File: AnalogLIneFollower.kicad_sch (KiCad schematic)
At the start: 28 parts, among them M1 Left Motor, M2 Right Motor, Q1 SS8050, Q2 SS8050, U1 LM358

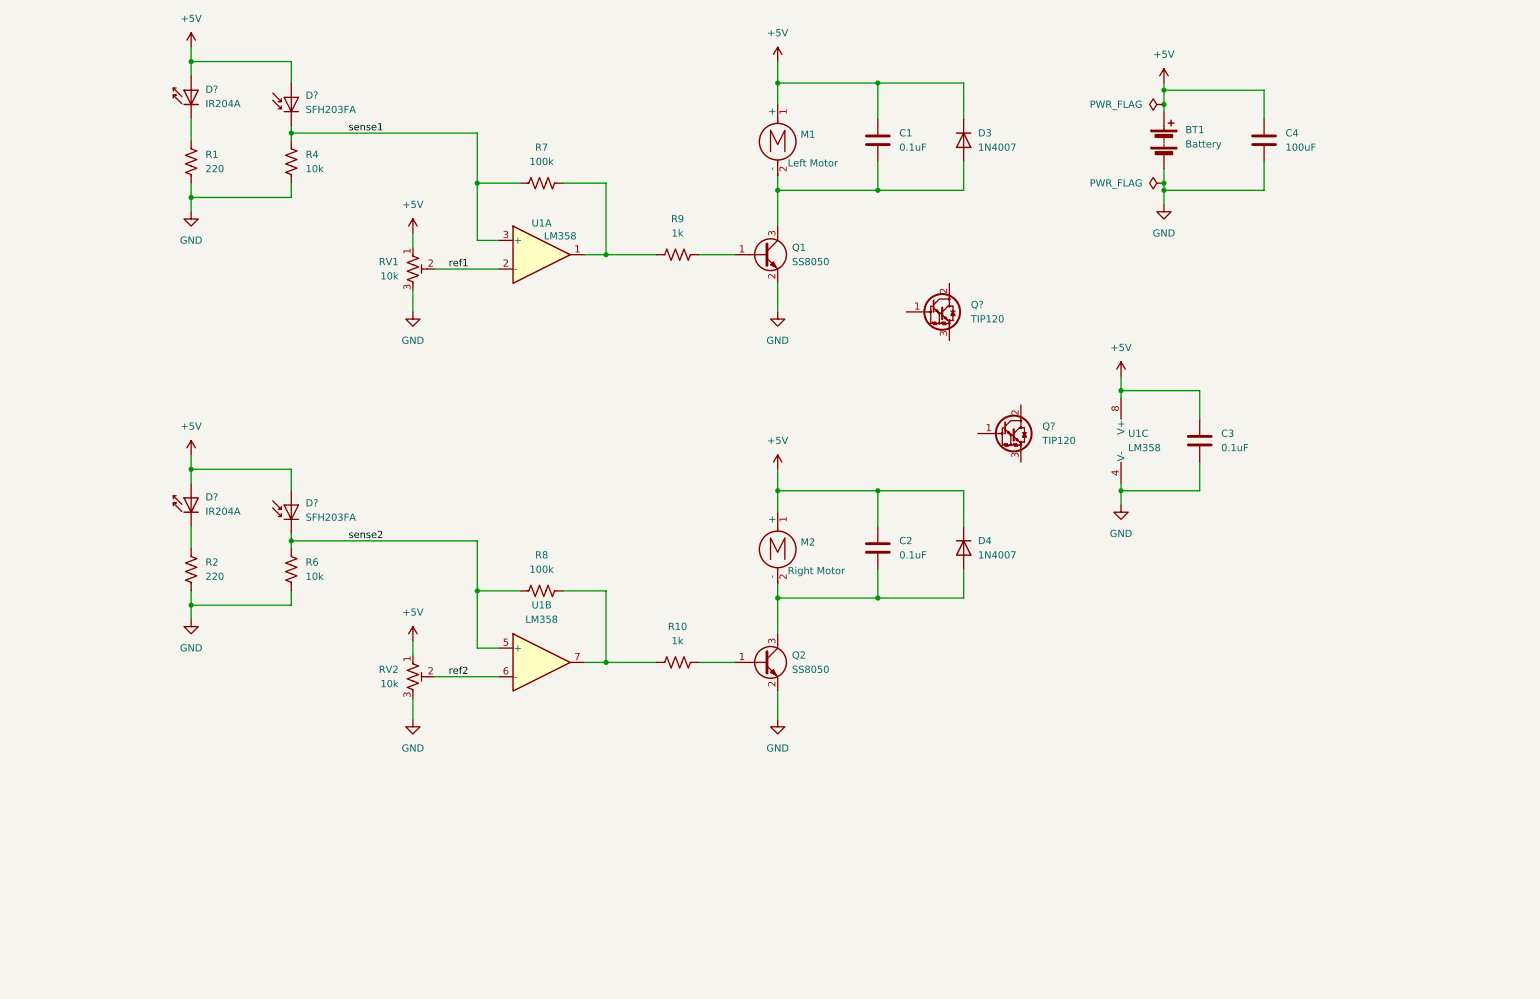
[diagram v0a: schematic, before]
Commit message: update schematic with new components
added decoupling and bulk capacitors
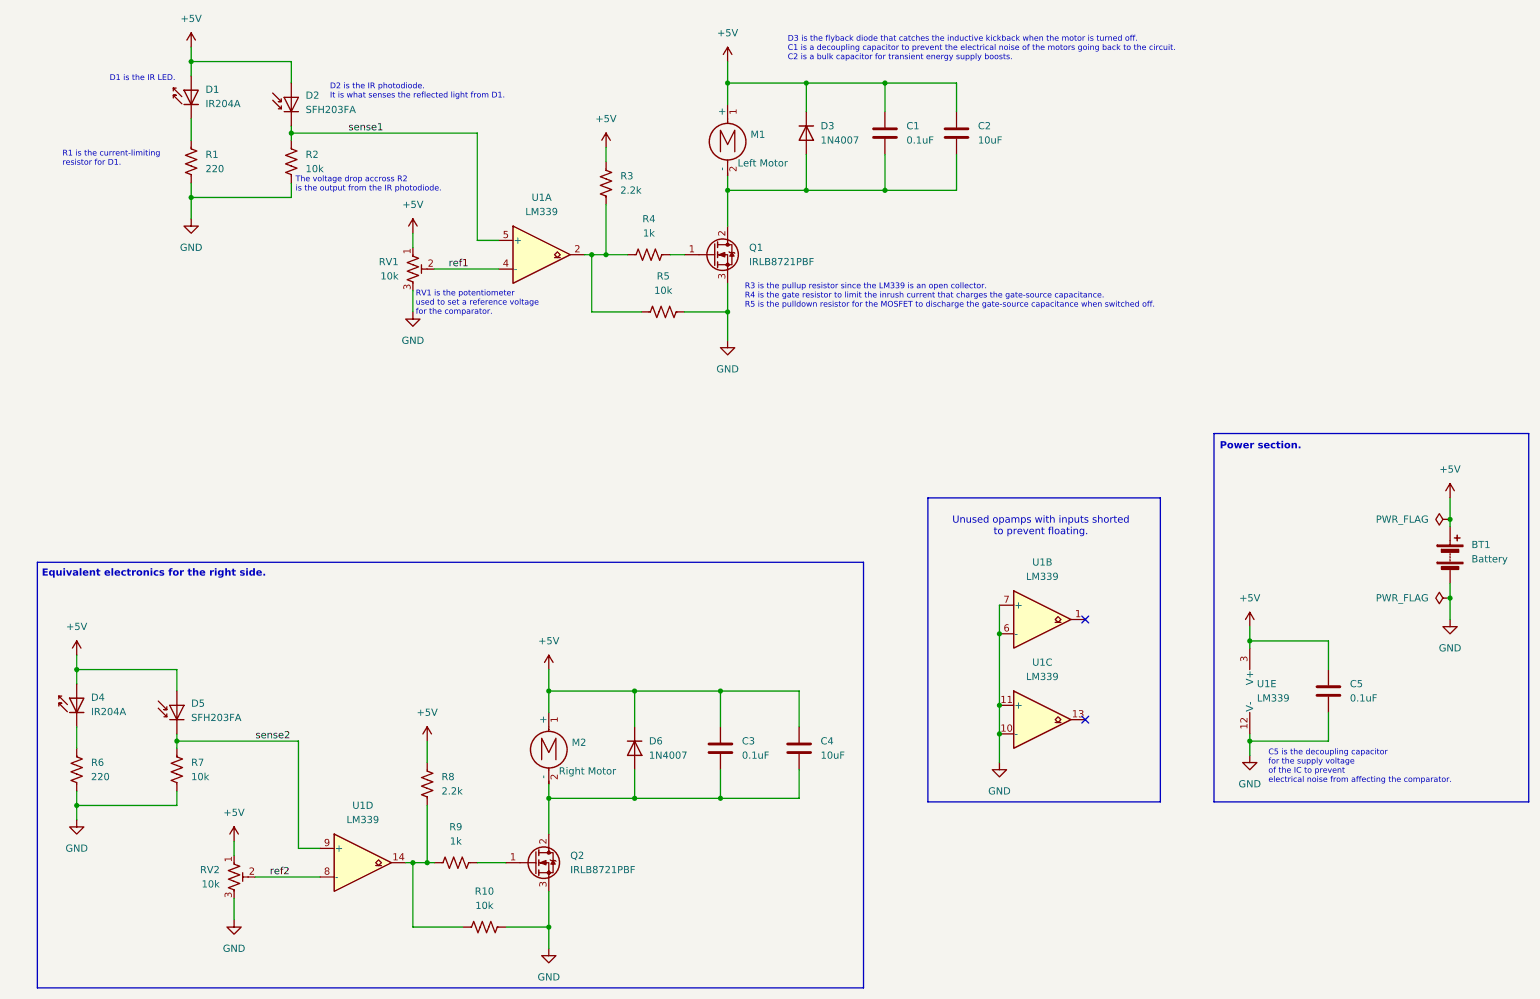
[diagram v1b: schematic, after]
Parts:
- removed Q1, Q2: SS8050, Package_TO_SOT_THT:TO-92, symbol Transistor_BJT:SS8050
- removed Q? (x2): TIP120, Package_TO_SOT_THT:TO-220-3_Vertical, symbol Transistor_BJT:TIP120
- removed R7: 100k, Resistor_THT:R_Axial_DIN0309_L9.0mm_D3.2mm_P2.54mm_Vertical, symbol Device:R_US
- removed U1: LM358, Package_DIP:DIP-8_W7.62mm, symbol Amplifier_Operational:LM358
- added C5: 0.1uF, symbol Device:C
- added Q1, Q2: IRLB8721PBF, Package_TO_SOT_THT:TO-220-3_Vertical, symbol Transistor_FET:IRLB8721PBF
- added R10, R5: 10k, Resistor_THT:R_Axial_DIN0309_L9.0mm_D3.2mm_P2.54mm_Vertical, symbol Device:R_US
- added R3: 2.2k, Resistor_THT:R_Axial_DIN0309_L9.0mm_D3.2mm_P2.54mm_Vertical, symbol Device:R_US
- added U1: LM339, symbol Comparator:LM339
- C1, C3: footprint Capacitor_THT:C_Radial_D6.3mm_H5.0mm_P2.50mm -> (none)
- C2: value 0.1uF -> 10uF; footprint Capacitor_THT:C_Radial_D6.3mm_H5.0mm_P2.50mm -> (none)
- C4: value 100uF -> 10uF; footprint Capacitor_THT:C_Radial_D6.3mm_H11.0mm_P2.50mm -> (none)
- R8: value 100k -> 2.2k
- gave numbers to parts that had none: 4
- renumbered D4 to D6, R4 to R2, R9 to R4, R2 to R6, R6 to R7, R10 to R9
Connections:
- net +5V: now also R8.2, C5.1, R3.2, U1.3 (V+)
- net GND: now also C5.2, Q1.3 (S), Q2.3 (S), R10.2, R5.2, U1.10 (-), U1.11 (+), U1.12 (V-), U1.6 (-), U1.7 (+); no longer C3.2, C4.2
- net ref1: now also U1.4 (-)
- net ref2: now also U1.8 (-)
- net sense1: now also U1.5 (+)
- net sense2: now also U1.9 (+); no longer R8.1
- net at R9.1: now also R8.1, R10.1, U1.14; no longer R8.2
- net at R9.2: now also Q2.1 (G)
- net at D6.2 (A), M2.2 (-): now also C3.2, C4.2, Q2.2 (D); no longer C2.2
- net at R4.1: now also R3.1, R5.1, U1.2
- net at R4.2: now also Q1.1 (G)
- net at C1.2, D3.2 (A), M1.2 (-): now also C2.2, Q1.2 (D)
- no-connect marks 0 -> 2
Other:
- note added: "C5 is the decoupling capacitor for the supply voltage of the IC to prevent electrical noise from affecting the comparator."
- note added: "D1 is the IR LED."
- note added: "D2 is the IR photodiode. It is what senses the reflected light from D1."
- note added: "D3 is the flyback diode that catches the inductive kickback when the motor is turned off. C1 is a decoupling capacitor to prevent the electrical noise of the motors going back to the circuit. C2 is a bulk capacitor for transient energy supply boosts."
- note added: "Equivalent electronics for the right side."
- note added: "Power section."
- note added: "R1 is the current-limiting resistor for D1."
- note added: "R3 is the pullup resistor since the LM339 is an open collector. R4 is the gate resistor to limit the inrush current that charges the gate-source capacitance. R5 is the pulldown resistor for the MOSFET to discharge the gate-source capacitance when switched off."
- note added: "RV1 is the potentiometer used to set a reference voltage for the comparator."
- note added: "The voltage drop accross R2 is the output from the IR photodiode."
- note added: "Unused opamps with inputs shorted to prevent floating."
- moved on the sheet: BT1, D3, D4, D5, D6, M1, M2, R4, R6, R7, R9, RV2
